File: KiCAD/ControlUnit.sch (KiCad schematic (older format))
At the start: 27 parts, among them U602 74HCT08N, U603 74LS153, U605 74HCT244N, U606 74HCT273N, U607 74HCT273N, U608 74LS161AN, U609 74HCT244N, U610 AT28C64B, U611 AT28C64B, U612 AT28C64B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

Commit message: Moved SP out of register module into SP module; changed RS0 assert signal alias from RS0 to RSH; moved uCode and program code to different subdirs of Programming/ .
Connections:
- net RS0: no longer U610.19 (I/O7)
- new net RSH: U610.19 (I/O7)
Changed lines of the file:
@@
 CFL
 Text HLabel 14125 8750 2    50   Output ~ 0
-RS0
+RSH
 Text HLabel 14125 2600 2    50   Output ~ 0
 MAHI

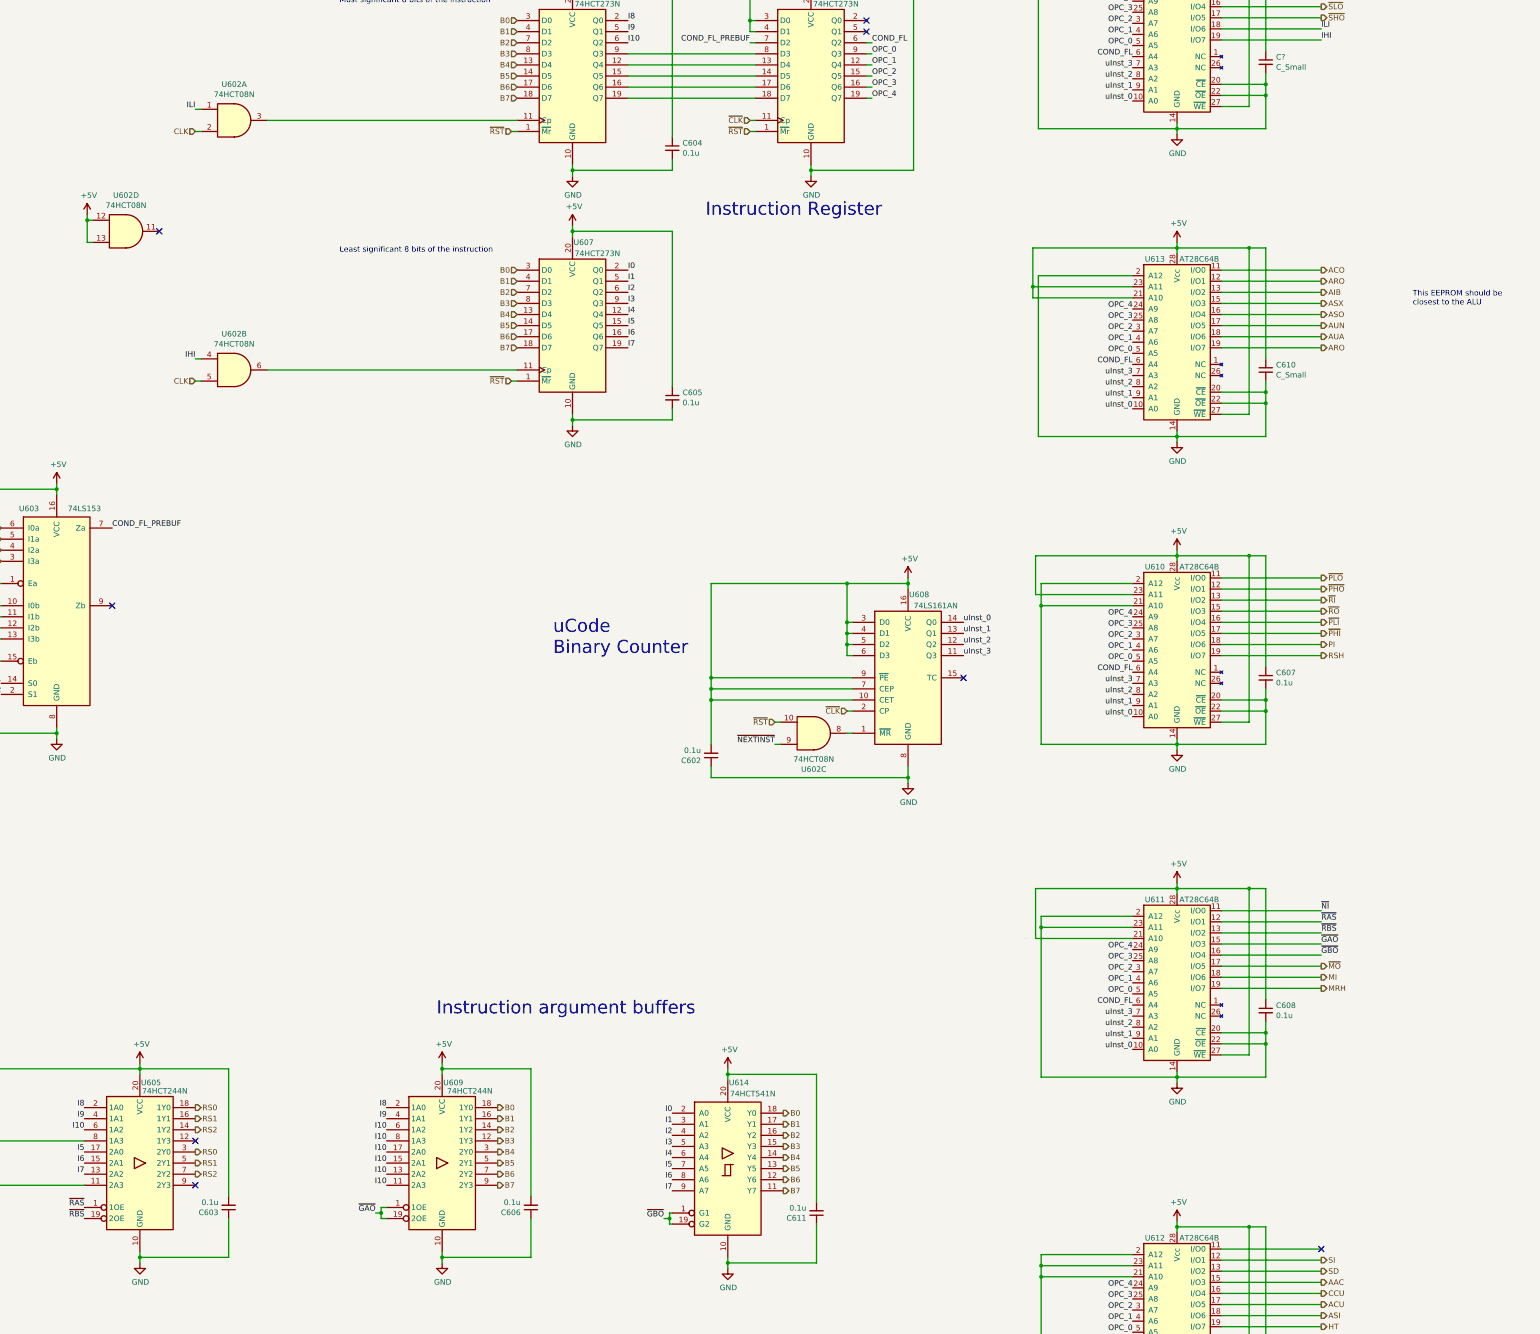
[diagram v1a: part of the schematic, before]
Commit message: First working versiongit add .  Added CSU control signal for updating C and O flags during add operations only.  Added circuitry to disable the reg decoder unless ~RI or ~RO are asserted.  Potential future issues: PC clock noise, reg clock noise, clock module being crap..
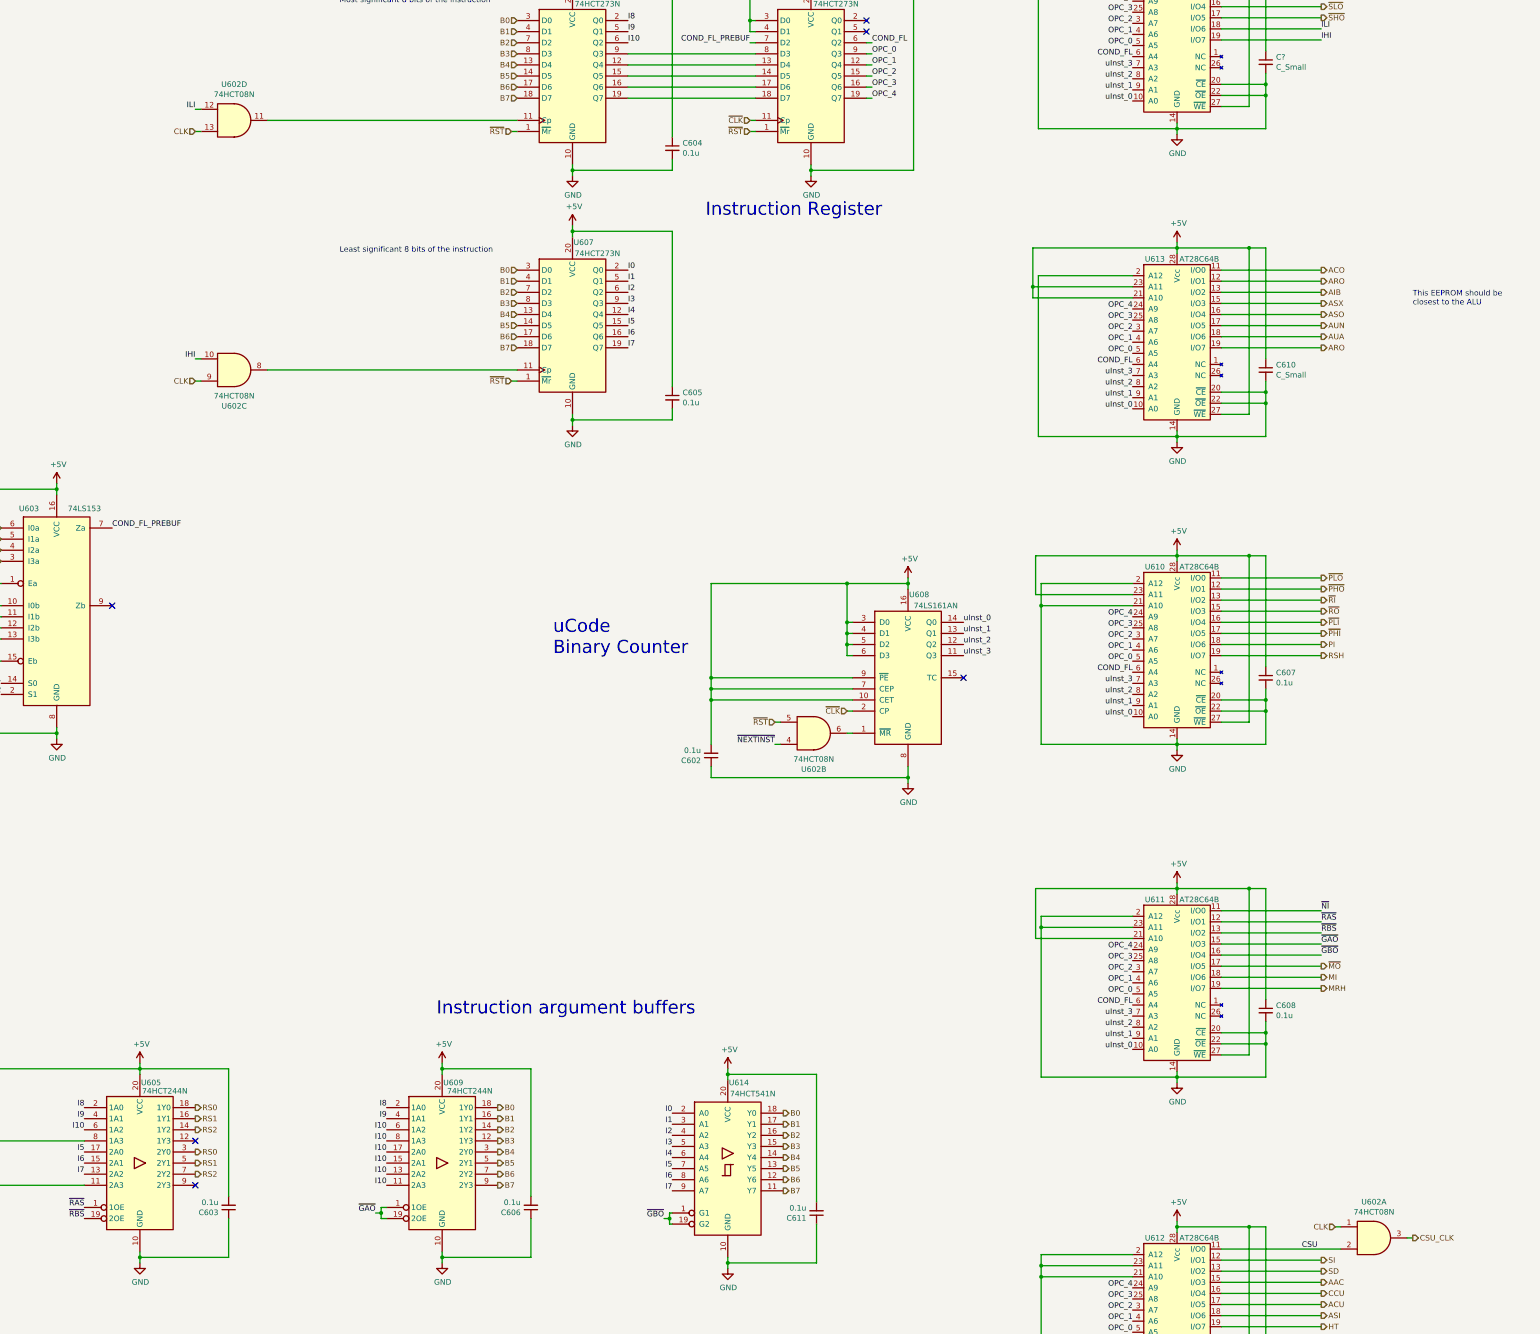
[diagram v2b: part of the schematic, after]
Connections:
- net +5V: no longer U602.12, U602.13
- net CLK: now also U602.1, U602.13, U602.9; no longer U602.2, U602.5
- net IHI: now also U602.10; no longer U602.4
- net ILI: now also U602.12; no longer U602.1
- net ~NEXTINST: now also U602.4; no longer U602.9
- net ~RST: now also U602.5; no longer U602.10
- net at U607.11 (Cp): now also U602.8; no longer U602.6
- net at U606.11 (Cp): now also U602.11; no longer U602.3
- net at U608.1 (~MR): now also U602.6; no longer U602.8
- net CSU: now reaches U612.11 (I/O0)
- net CSU: now also U602.2
- new net CSU_CLK: U602.3
- no-connect marks 8 -> 6
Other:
- moved on the sheet: U602A, U602B, U602C, U602D
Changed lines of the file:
@@
 Wire Wire Line
 	8625 9050 8625 9150
-Wire Wire Line
-	8625 9150 9900 9150
 Connection ~ 8625 9050
 Text Label 9200 9550 2    50   ~ 0
@@
 L Breadboard_CPU-rescue:74LS08-74xx U?
 U 1 1 618B5634
-P 4325 3925
+P 14600 14000
 AR Path="/5EFC06D4/618B5634" Ref="U?"  Part="1"
 AR Path="/5F05F116/618B5634" Ref="U602"  Part="1"
-F 0 "U602" H 4325 4250 50  0000 C CNN
-F 1 "74HCT08N" H 4325 4159 50  0000 C CNN
-F 2 "" H 4325 3925 50  0001 C CNN
-F 3 "http://www.ti.com/lit/gpn/sn74LS08" H 4325 3925 50  0001 C CNN
-	1    4325 3925
+F 0 "U602" H 14600 14325 50  0000 C CNN
+F 1 "74HCT08N" H 14600 14234 50  0000 C CNN
+F 2 "" H 14600 14000 50  0001 C CNN
+F 3 "http://www.ti.com/lit/gpn/sn74LS08" H 14600 14000 50  0001 C CNN
+	1    14600 14000
 	1    0    0    -1
 $EndComp
@@
 L Breadboard_CPU-rescue:74LS08-74xx U?
 U 2 1 618B563A
-P 4325 6175
+P 9550 9450
 AR Path="/5EFC06D4/618B563A" Ref="U?"  Part="2"
 AR Path="/5F05F116/618B563A" Ref="U602"  Part="2"
-F 0 "U602" H 4325 6500 50  0000 C CNN
-F 1 "74HCT08N" H 4325 6409 50  0000 C CNN
-F 2 "" H 4325 6175 50  0001 C CNN
-F 3 "http://www.ti.com/lit/gpn/sn74LS08" H 4325 6175 50  0001 C CNN
-	2    4325 6175
-	1    0    0    -1
+F 0 "U602" H 9550 9775 50  0000 C CNN
+F 1 "74HCT08N" H 9550 9684 50  0000 C CNN
+F 2 "" H 9550 9450 50  0001 C CNN
+F 3 "http://www.ti.com/lit/gpn/sn74LS08" H 9550 9450 50  0001 C CNN
+	2    9550 9450
+	1    0    0    1
 $EndComp
 $Comp
@@
 L Breadboard_CPU-rescue:74LS08-74xx U?
 U 3 1 618B5640
-P 9550 9450
+P 4325 6175
 AR Path="/5EFC06D4/618B5640" Ref="U?"  Part="3"
 AR Path="/5F05F116/618B5640" Ref="U602"  Part="3"
-F 0 "U602" H 9550 9775 50  0000 C CNN
-F 1 "74HCT08N" H 9550 9684 50  0000 C CNN
-F 2 "" H 9550 9450 50  0001 C CNN
-F 3 "http://www.ti.com/lit/gpn/sn74LS08" H 9550 9450 50  0001 C CNN
-	3    9550 9450
+F 0 "U602" H 4325 6500 50  0000 C CNN
+F 1 "74HCT08N" H 4325 6409 50  0000 C CNN
+F 2 "" H 4325 6175 50  0001 C CNN
+F 3 "http://www.ti.com/lit/gpn/sn74LS08" H 4325 6175 50  0001 C CNN
+	3    4325 6175
 	1    0    0    1
 $EndComp
@@
 Wire Wire Line
 	14125 14200 13225 14200
-Wire Wire Line
-	14125 14100 13225 14100
 Wire Wire Line
 	14125 14400 13225 14400
@@
 L Breadboard_CPU-rescue:74LS08-74xx U?
 U 4 1 618B5646
-P 3350 4925
+P 4325 3925
 AR Path="/5EFC06D4/618B5646" Ref="U?"  Part="4"
 AR Path="/5F05F116/618B5646" Ref="U602"  Part="4"
-F 0 "U602" H 3350 5250 50  0000 C CNN
-F 1 "74HCT08N" H 3350 5159 50  0000 C CNN
-F 2 "" H 3350 4925 50  0001 C CNN
-F 3 "http://www.ti.com/lit/gpn/sn74LS08" H 3350 4925 50  0001 C CNN
-	4    3350 4925
+F 0 "U602" H 4325 4250 50  0000 C CNN
+F 1 "74HCT08N" H 4325 4159 50  0000 C CNN
+F 2 "" H 4325 3925 50  0001 C CNN
+F 3 "http://www.ti.com/lit/gpn/sn74LS08" H 4325 3925 50  0001 C CNN
+	4    4325 3925
 	1    0    0    -1
 $EndComp
@@
 Text HLabel 9200 9350 0    50   Input ~ 0
 ~RST
-NoConn ~ 3650 4925
 Wire Wire Line
 	11575 4000 12825 4000
@@
 Text HLabel 14125 11750 2    50   Output ~ 0
 MRH
-NoConn ~ 14125 14100
 Wire Wire Line
 	1325 9450 1875 9450
@@
 $Comp
 L power:+5V #PWR?
-U 1 1 61A7388E
-P 3000 4775
-F 0 "#PWR?" H 3000 4625 50  0001 C CNN
-F 1 "+5V" H 3015 4948 50  0000 C CNN
-F 2 "" H 3000 4775 50  0001 C CNN
-F 3 "" H 3000 4775 50  0001 C CNN
-	1    3000 4775
-	1    0    0    -1
-$EndComp
-Wire Wire Line
-	3000 4775 3000 4825
-Wire Wire Line
-	3000 5025 3050 5025
-Wire Wire Line
-	3000 4825 3050 4825
-Connection ~ 3000 4825
-Wire Wire Line
-	3000 4825 3000 5025
-$Comp
-L power:+5V #PWR?
 U 1 1 61ACB395
 P 7375 2625
@@
 	1    0    0    -1
 $EndComp
+Wire Wire Line
+	8625 9150 9900 9150
+Wire Wire Line
+	13225 14100 14300 14100
+Text HLabel 14250 13900 0    50   Input ~ 0
+CLK
+Wire Wire Line
+	14250 13900 14300 13900
+Wire Wire Line
+	14900 14000 14950 14000
+Text Label 13950 14100 0    50   ~ 0
+CSU
+Text HLabel 14950 14000 2    50   Output ~ 0
+CSU_CLK
 $EndSCHEMATC
